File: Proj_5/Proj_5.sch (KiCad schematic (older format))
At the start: 0 parts

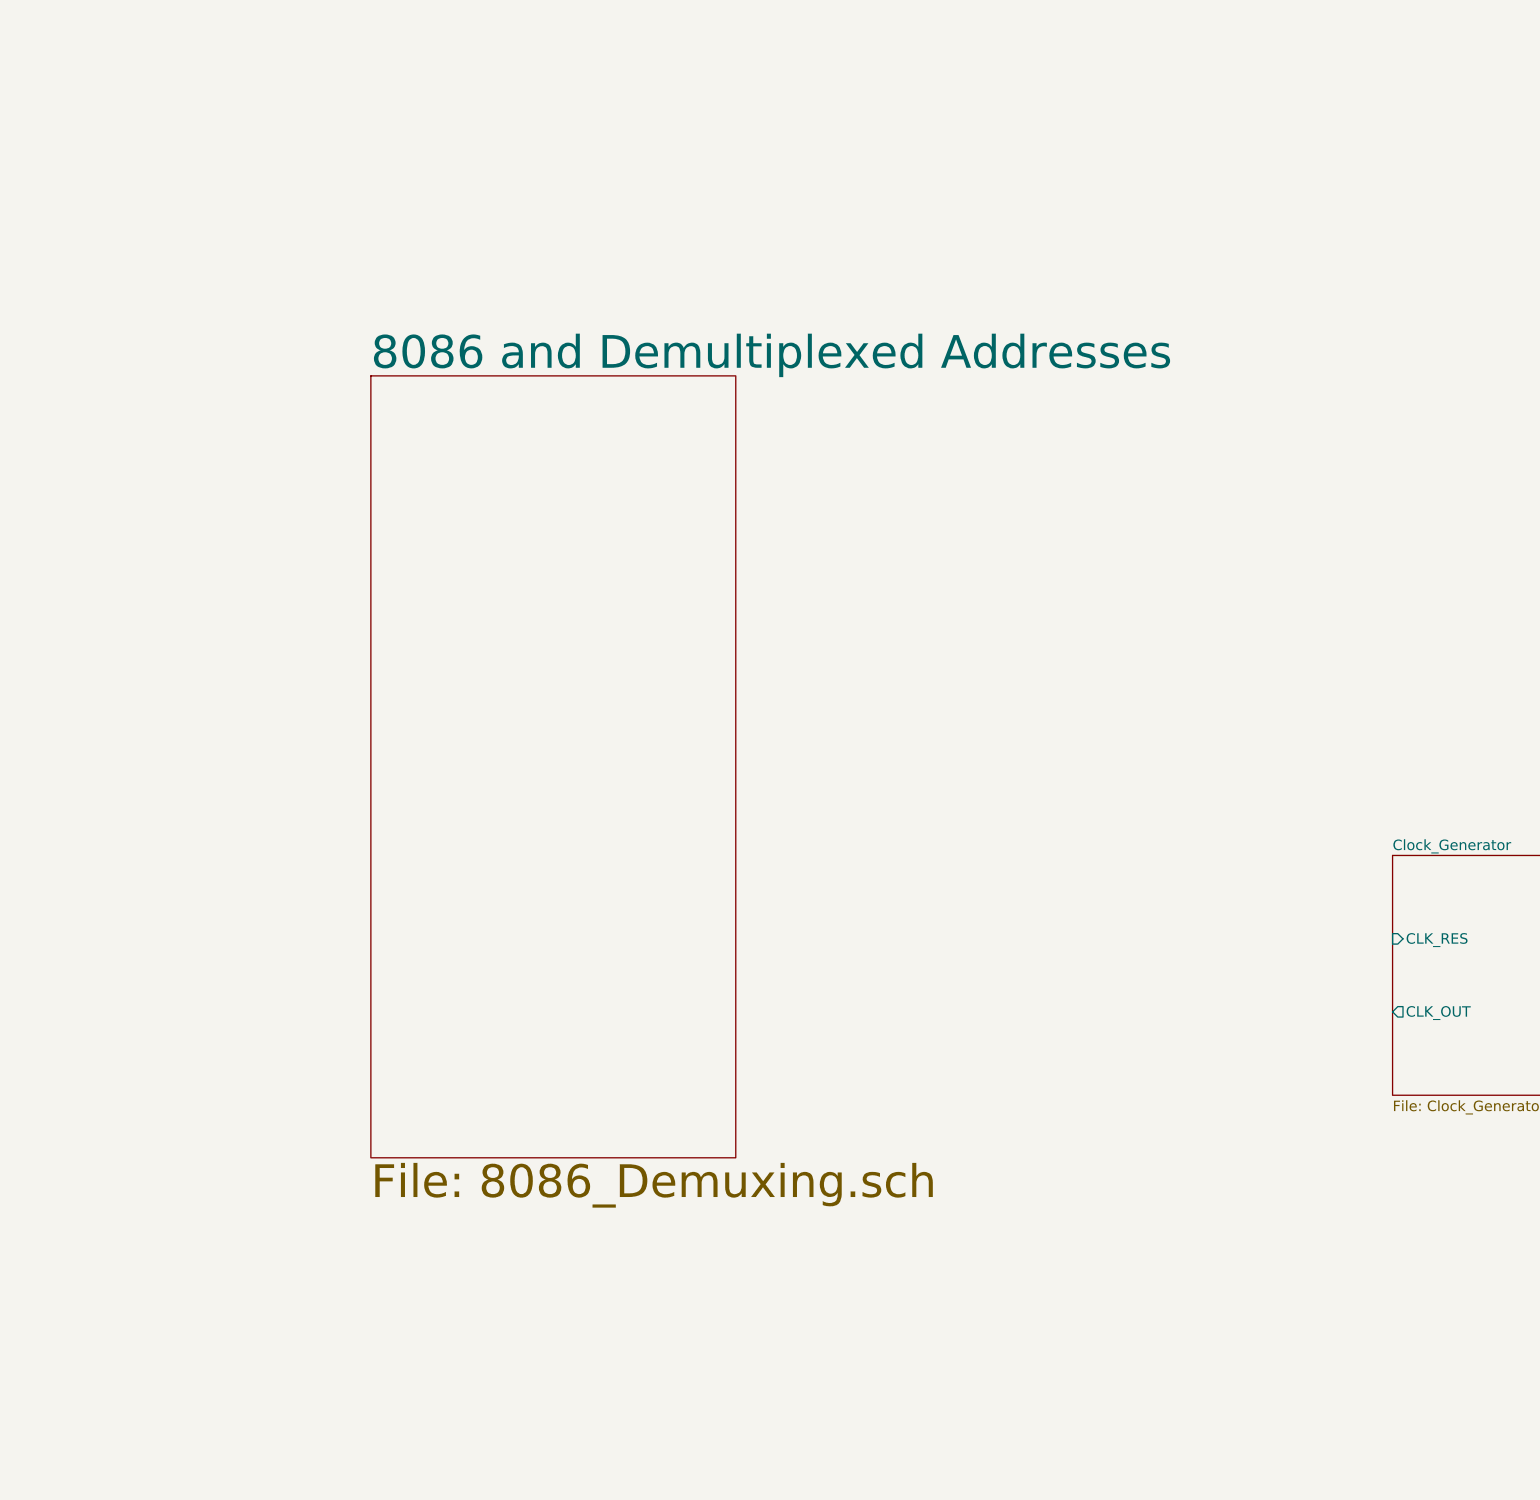
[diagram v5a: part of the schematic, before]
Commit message: Progress on 8279
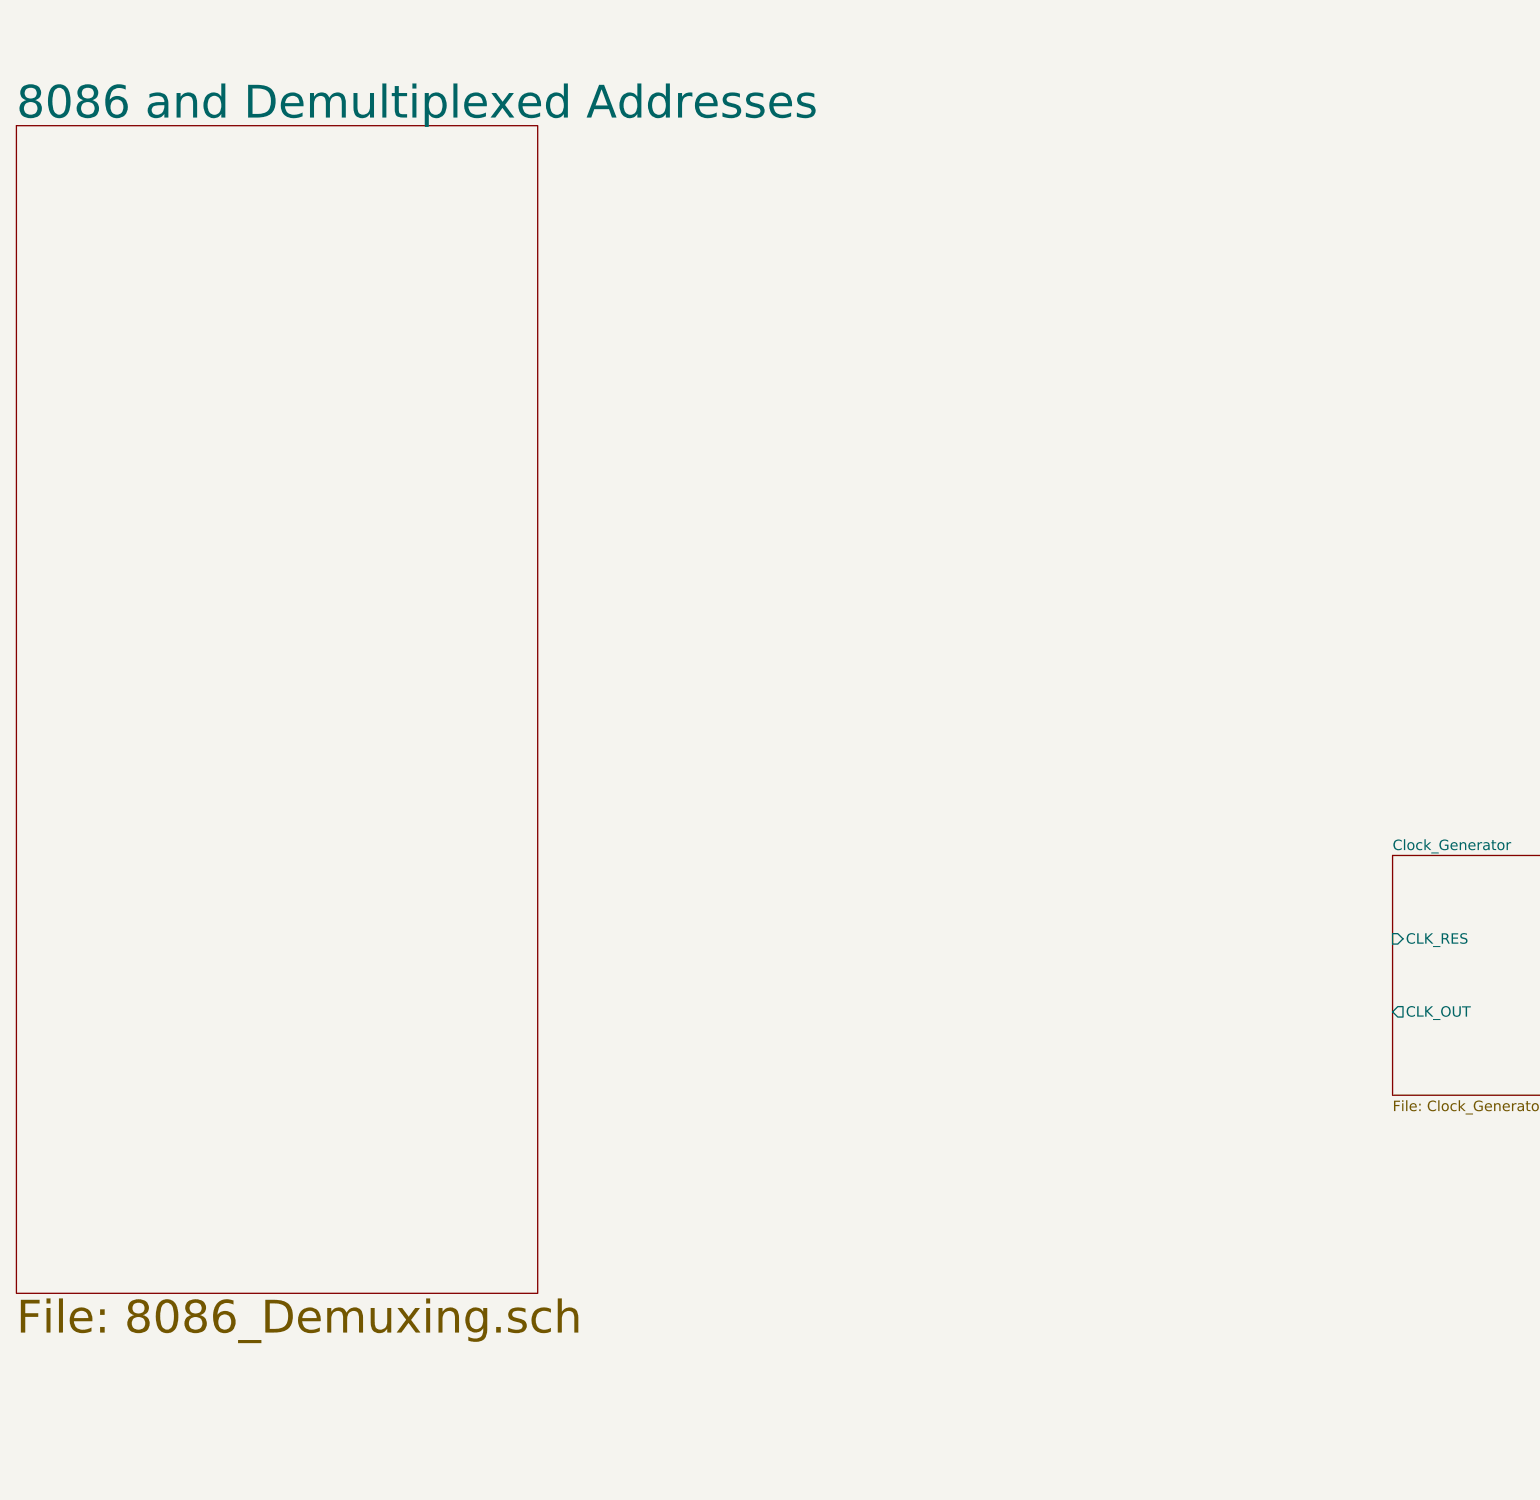
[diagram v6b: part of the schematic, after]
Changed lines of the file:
@@
 Ryan Bugianesi and Collin Mood\n
 $Sheet
-S 4500 2450 1750 3750
+S 2800 1250 2500 5600
 U 5E9F3A3D
 F0 "8086 and Demultiplexed Addresses" 157
